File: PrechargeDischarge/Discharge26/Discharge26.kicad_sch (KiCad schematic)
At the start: 11 parts, among them J1 HV_Conn, J2 LV_Conn, K4 Relay_SPST-NC, Q1 Q_NMOS_GSD

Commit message: changes mounting holes on discharge to M4
gareth wants all pcb mounting holes to M4
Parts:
- H1, H2, H3, H4: footprint MountingHole:MountingHole_2.2mm_M2 -> MountingHole:MountingHole_4.3mm_M4
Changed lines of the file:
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@@
 			)
 		)
-		(property "Footprint" "MountingHole:MountingHole_2.2mm_M2"
+		(property "Footprint" "MountingHole:MountingHole_4.3mm_M4"
 			(at 54.61 22.86 0)
 			(effects
@@
 			)
 		)
-		(property "Footprint" "MountingHole:MountingHole_2.2mm_M2"
+		(property "Footprint" "MountingHole:MountingHole_4.3mm_M4"
 			(at 91.44 22.86 0)
 			(effects
@@
 			)
 		)
-		(property "Footprint" "MountingHole:MountingHole_2.2mm_M2"
+		(property "Footprint" "MountingHole:MountingHole_4.3mm_M4"
 			(at 34.29 22.86 0)
 			(effects
@@
 			)
 		)
-		(property "Footprint" "MountingHole:MountingHole_2.2mm_M2"
+		(property "Footprint" "MountingHole:MountingHole_4.3mm_M4"
 			(at 72.39 22.86 0)
 			(effects

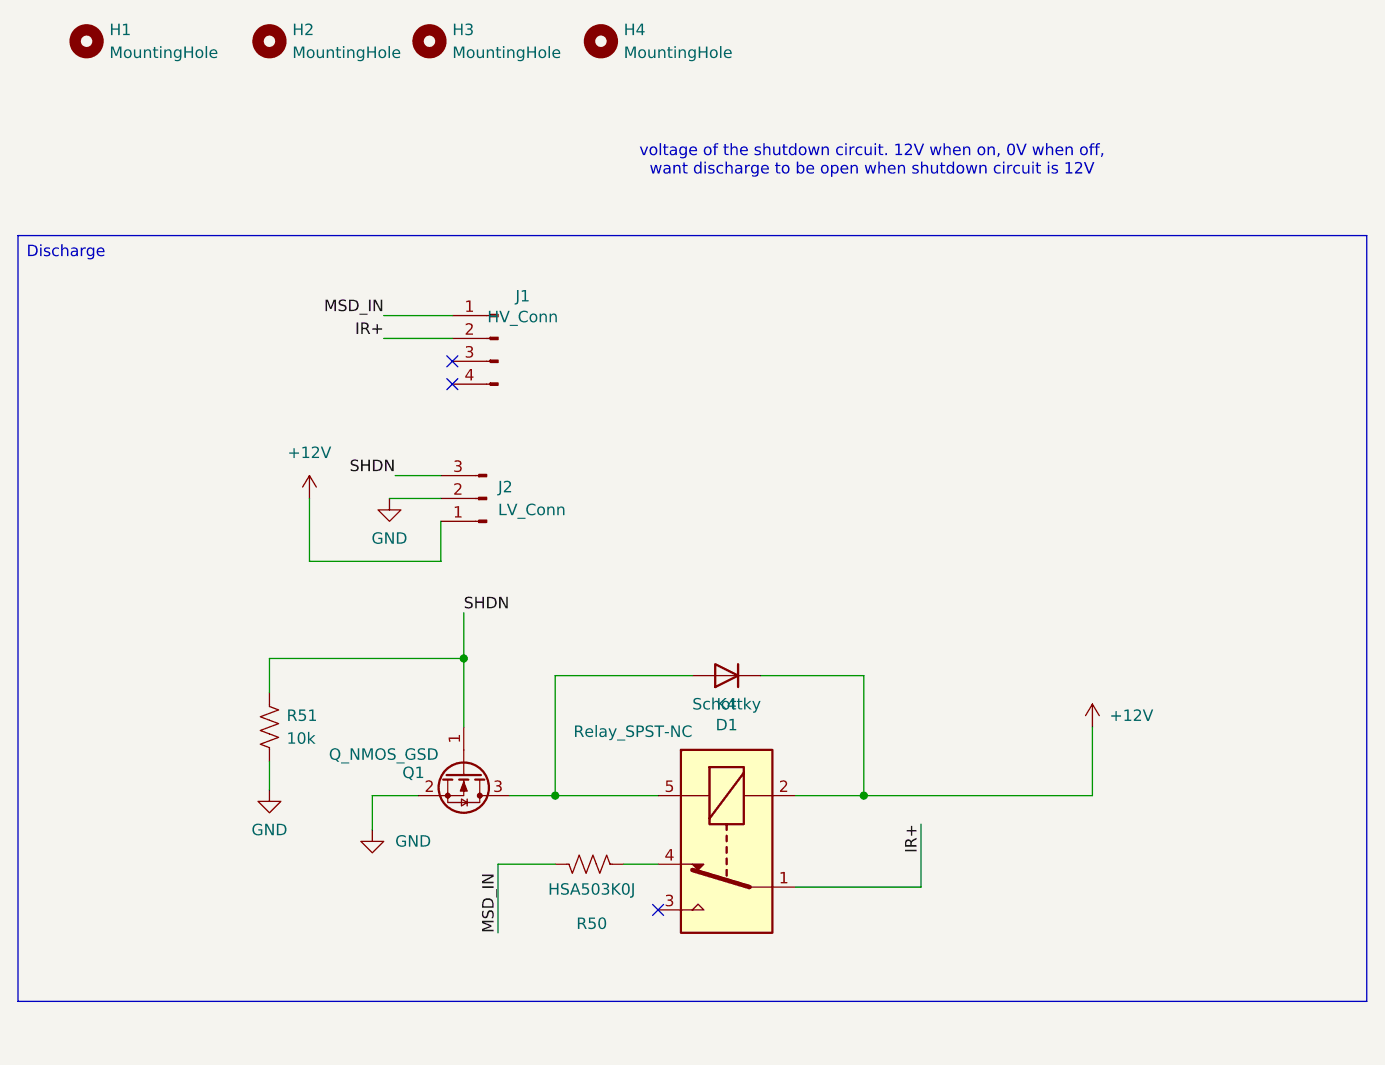
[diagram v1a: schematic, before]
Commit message: Discharge
Added through hole mosfets and LED driver to DIscharge board
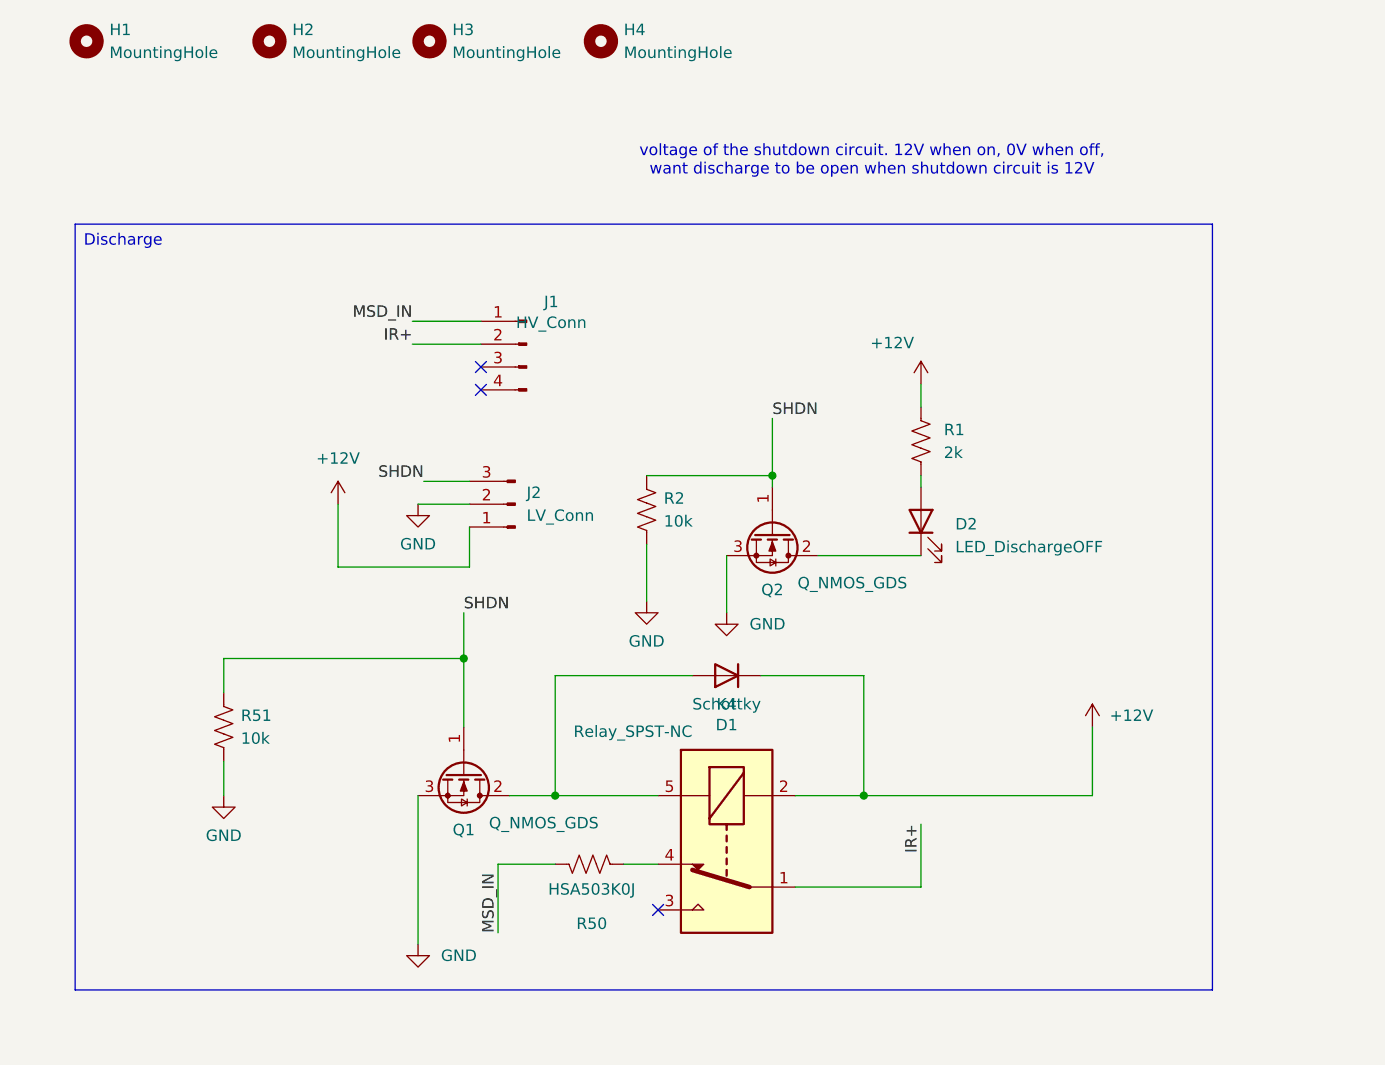
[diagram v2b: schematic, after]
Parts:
- removed Q1: Q_NMOS_GSD, Package_TO_SOT_SMD:SOT-23, symbol Transistor_FET:Q_NMOS_GSD
- added D2: LED_DischargeOFF, LED_SMD:LED_0805_2012Metric_Pad1.15x1.40mm_HandSolder, symbol Device:LED
- added Q1, Q2: Q_NMOS_GDS, Package_TO_SOT_THT:TO-251-3_Vertical, symbol Transistor_FET:Q_NMOS_GDS
- added R1: 2k, Resistor_SMD:R_0805_2012Metric_Pad1.20x1.40mm_HandSolder, symbol Device:R_US
- added R2: 10k, Resistor_SMD:R_1206_3216Metric, symbol Device:R_US
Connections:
- net +12V: now also R1.1
- net GND: now also Q1.3 (S), Q2.3 (S), R2.2
- net SHDN: now also Q1.1 (G), Q2.1 (G), R2.1
- net at D1.2 (A), K4.5: now also Q1.2 (D)
- new net: D2.2 (A), R1.2
- new net: D2.1 (K), Q2.2 (D)
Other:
- moved on the sheet: J1, J2, R51

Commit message: discharge fixed
added zener diode from nmos gate to source, also added indiactor LED
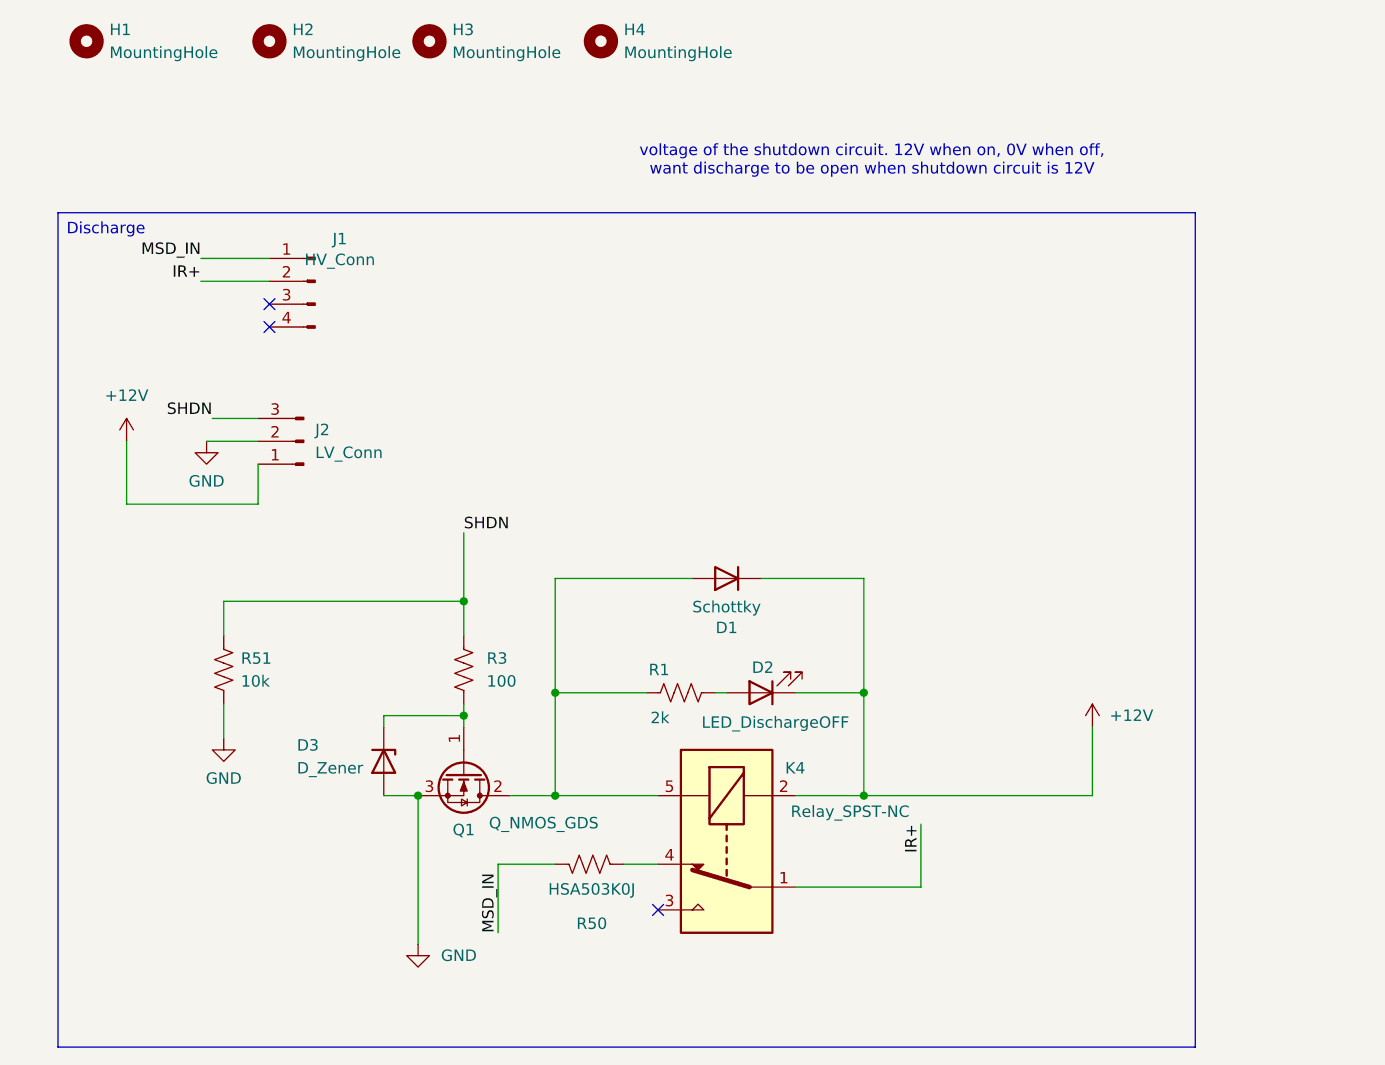
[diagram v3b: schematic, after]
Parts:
- removed Q2: Q_NMOS_GDS, Package_TO_SOT_THT:TO-251-3_Vertical, symbol Transistor_FET:Q_NMOS_GDS
- removed R2: 10k, Resistor_SMD:R_1206_3216Metric, symbol Device:R_US
- added D3: D_Zener, Diode_SMD:D_SOD-123, symbol Device:D_Zener
- added R3: 100, Resistor_SMD:R_0805_2012Metric_Pad1.20x1.40mm_HandSolder, symbol Device:R_US
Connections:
- net +12V: now also D2.1 (K); no longer R1.1
- net GND: now also D3.2 (A)
- net SHDN: now also R3.1; no longer Q1.1 (G)
- net at D1.2 (A), K4.5, Q1.2 (D): now also R1.1
- new net: D3.1 (K), Q1.1 (G), R3.2
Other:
- moved on the sheet: D1, D2, J1, J2, R1, R51

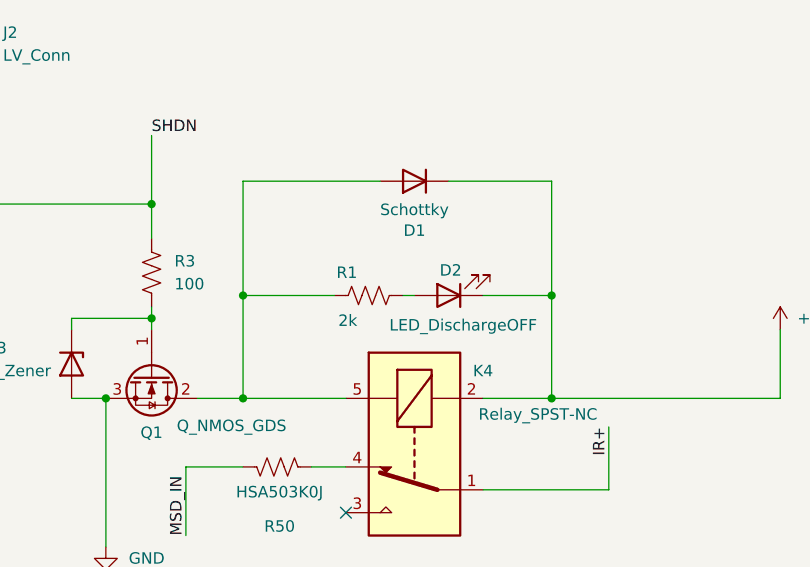
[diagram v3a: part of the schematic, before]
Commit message: Fixed Discharge + Added RML Quick files
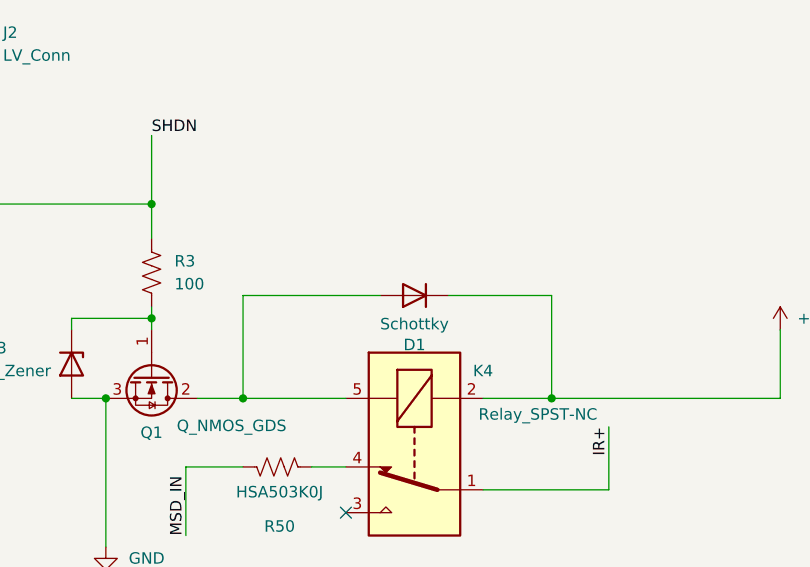
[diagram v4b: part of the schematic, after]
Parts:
- removed D2: LED_DischargeOFF, LED_SMD:LED_0805_2012Metric_Pad1.15x1.40mm_HandSolder, symbol Device:LED
- removed R1: 2k, Resistor_SMD:R_0805_2012Metric_Pad1.20x1.40mm_HandSolder, symbol Device:R_US
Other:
- moved on the sheet: D1
